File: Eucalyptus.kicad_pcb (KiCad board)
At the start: 2 copper layers, 60 x 35 mm, 59 parts, among them J1 HEADER_2, J10 ICSP, J11 HEADER_1, J12 HEADER_1, J13 HEADER_1, J14 HEADER_1, J15 HEADER_1, J16 HEADER_2, J17 HEADER_2, J2 Transmisor RF, J3 HEADER_1, J4 HEADER_1, J5 HEADER_1, J6 HEADER_1, J7 HEADER_1, J8 HEADER_1, J9 HEADER_1, Q1 2N7002, SW1 SW_PUSH, SW2 SW_PUSH, SW3 Estrategias, U1 LM1117-SOT, U2 ATMEGA328P-AU, U3 DRV8872, U4 DRV8872, Y1 Crystal

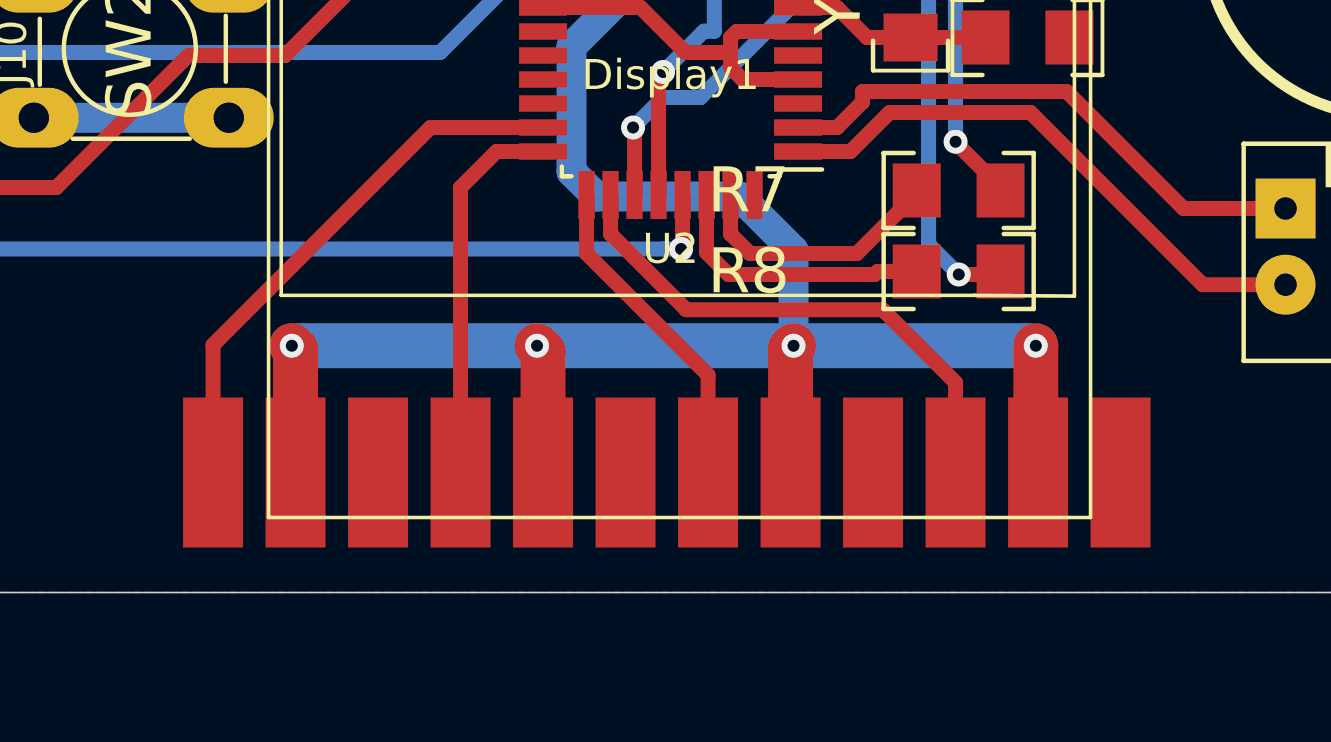
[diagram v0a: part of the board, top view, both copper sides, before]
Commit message: DualPad
Modifique y acomode los footprints de los sensores
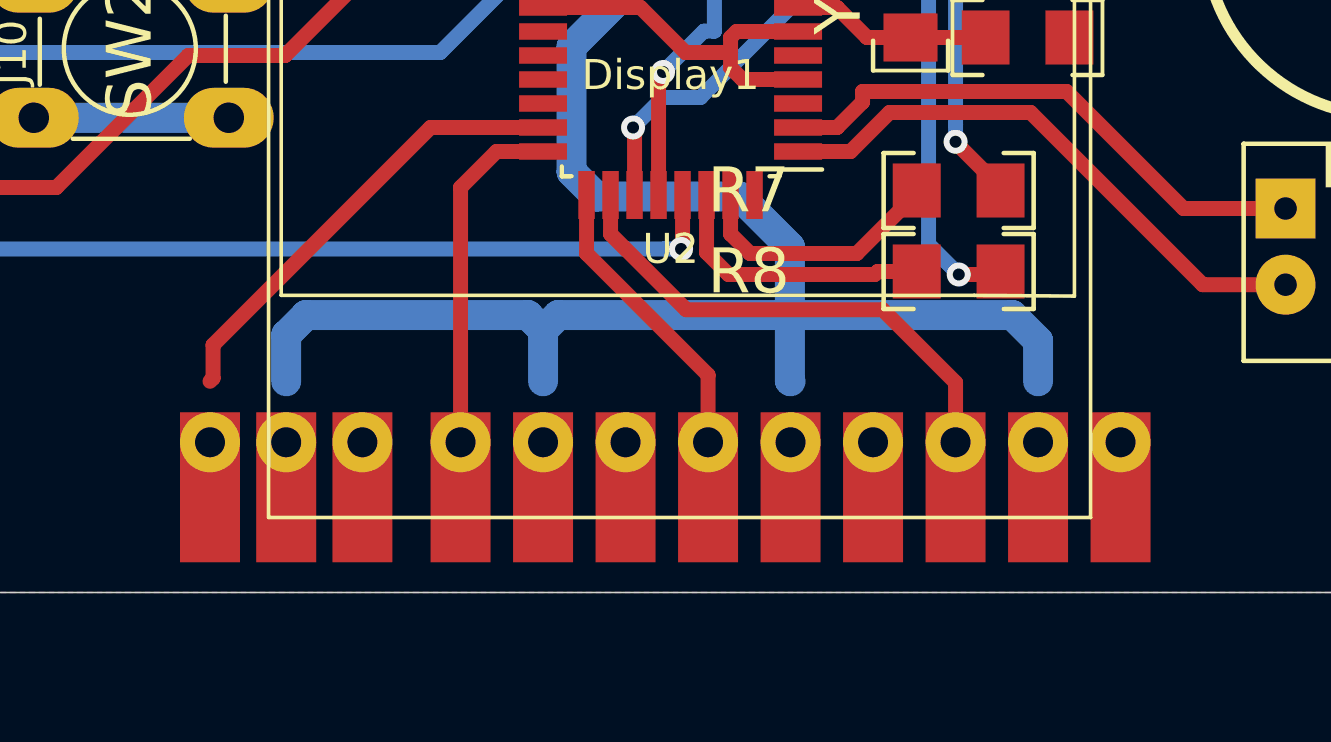
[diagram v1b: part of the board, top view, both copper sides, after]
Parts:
- J11, J12, J13, J14, J15, J3, J4, J5, J6, J7, J8, J9: footprint EESTN5:PAD_SMD_2x5mm -> EESTN5:DUAL_PAD_TH_SMD_2x5mm
- moved J9 0.72 mm to (109.7, 126.5), turned to 0 degrees
- moved J11 0.58 mm to (107.2, 126.5), turned to 0 degrees
- moved J5 0.50 mm to (104.6, 126.5)
- moved J12 0.49 mm to (121.2, 126.5)
- moved J13 0.49 mm to (118.5, 126.5), turned to 0 degrees
- moved J14 0.49 mm to (115.8, 126.5), turned to 0 degrees
- moved J15 0.49 mm to (113.0, 126.5)
- moved J3 0.49 mm to (135.0, 126.5)
- moved J4 0.49 mm to (132.2, 126.5)
- moved J6 0.49 mm to (126.8, 126.5)
- moved J7 0.49 mm to (124.0, 126.5)
- moved J8 0.49 mm to (129.5, 126.5)
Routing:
- net +5V: track 115.9 -> 106.0 mm, vias 4 -> 0
- net /DISTANCIA_I: track 19.3 -> 15.3 mm
- net /DISTANCIA_FI: track 13.7 -> 11.2 mm
- net /DISTANCIA_FD: track 11.9 -> 9.39 mm
- net /DISTANCIA_D: track 18.9 -> 16.3 mm

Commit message: MODIFICACIONES
SE MODIFICO LISTA DE MATERIALES Y EL PCB
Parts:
- C1, C11, C13, C14, C15, C3, D1, R10, R4, R5, R9, U1: moved to B.Cu
- moved C6 137.5 mm to (46.9, 99.8)
- moved R3 137.5 mm to (46.9, 103.5)
- moved SW1 113.8 mm to (166.4, 121.9), turned to 90 degrees
- moved C3 113.4 mm to (103.3, 104.1), turned to 90 degrees
- moved C11 110.5 mm to (100.5, 104.3), turned to 270 degrees
- moved C15 96.2 mm to (111.2, 101.7), turned to 90 degrees
- moved R10 94.6 mm to (121.3, 115.3), turned to 270 degrees
- moved U1 89.7 mm to (137.1, 102.8), turned to 90 degrees
- moved C14 82.0 mm to (140.8, 110.9)
- moved C13 66.6 mm to (135.4, 110.0), turned to 90 degrees
- moved C1 61.9 mm to (172.2, 100.5)
- moved R5 48.8 mm to (134.4, 119.9), turned to 270 degrees
- moved R4 46.0 mm to (136.9, 119.9), turned to 270 degrees
- moved R9 22.2 mm to (120.1, 108.2), turned to 180 degrees
- moved D1 13.7 mm to (144.0, 108.2), turned to 180 degrees
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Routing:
- net +5V: track 106.0 -> 144.2 mm
- net Net-(BZ1-Pad2): track 16.4 -> 2.98 mm
- net /AUX2: track 18.6 -> 27.0 mm
- net /Vin: track 53.7 -> 61.5 mm
- net /AUX1: track 19.2 -> 23.6 mm
- net /DISTANCIA_I: track 15.3 -> 18.8 mm
- net /BUZZER: track 1.99 -> 0.00 mm
- net /SDA: track 17.8 -> 19.2 mm

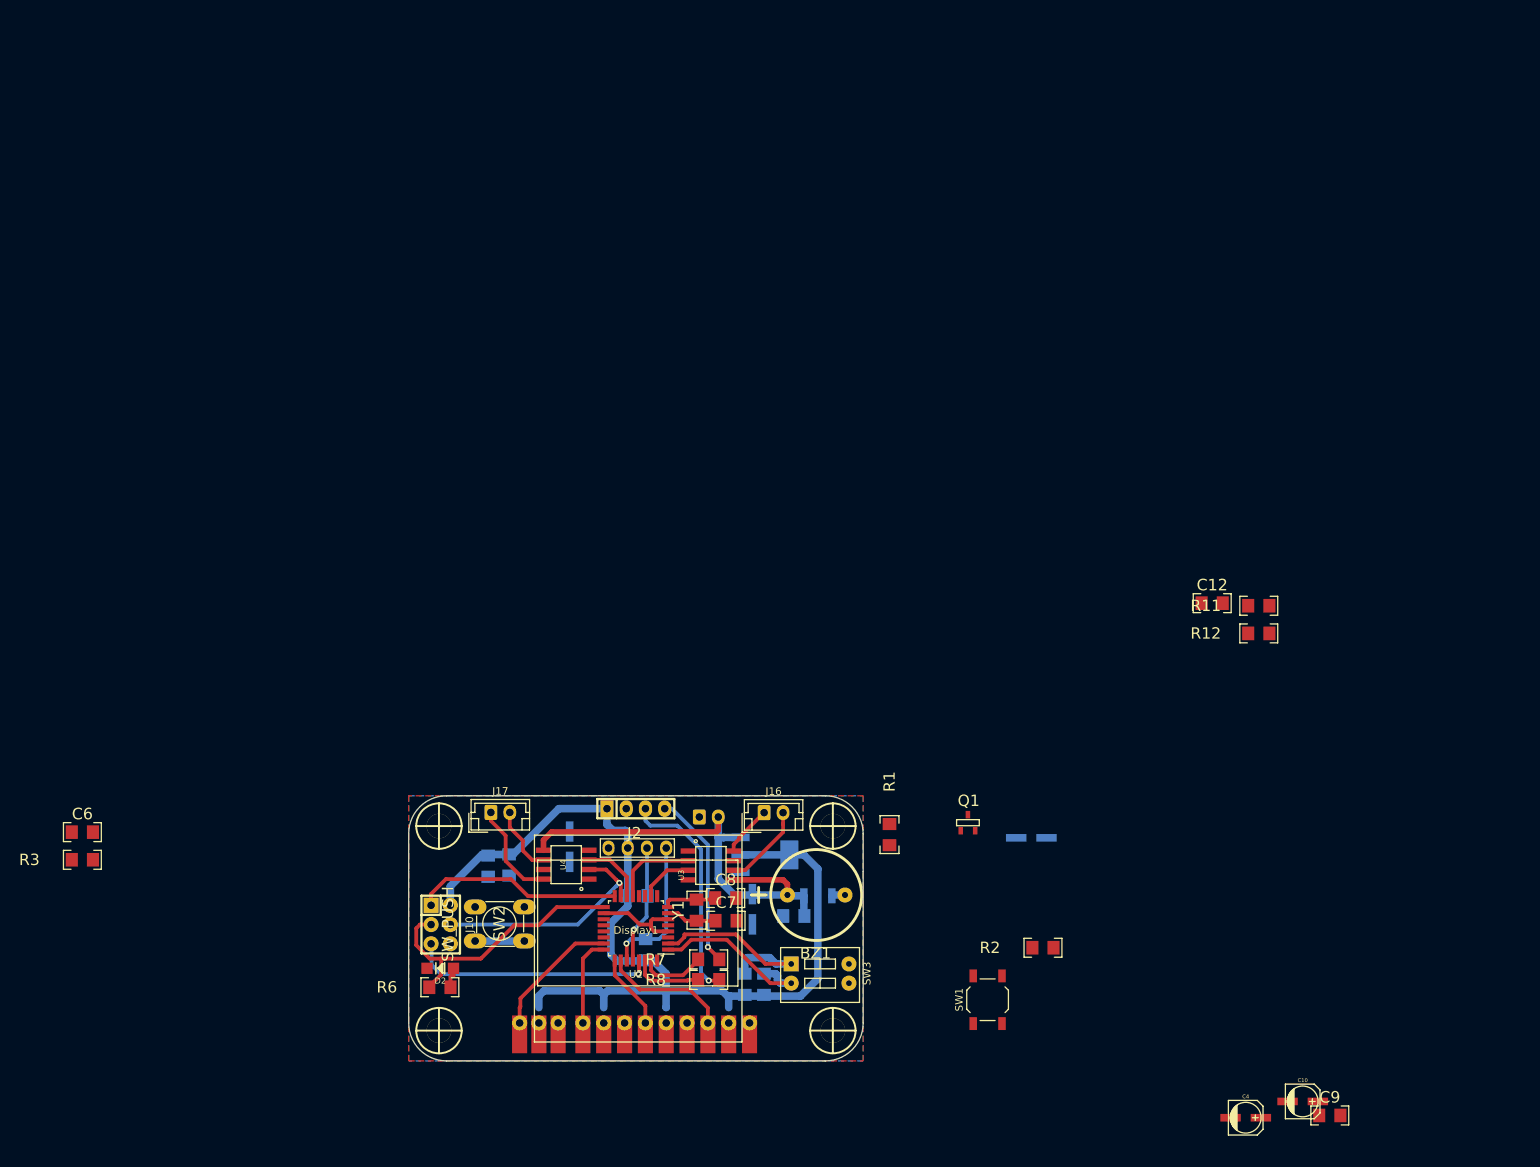
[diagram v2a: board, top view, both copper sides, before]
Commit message: modificaciones
se termino el pcb, modifique el cristal en e sch, termine lista de compnentes y genere 2 imagenes de la pcb
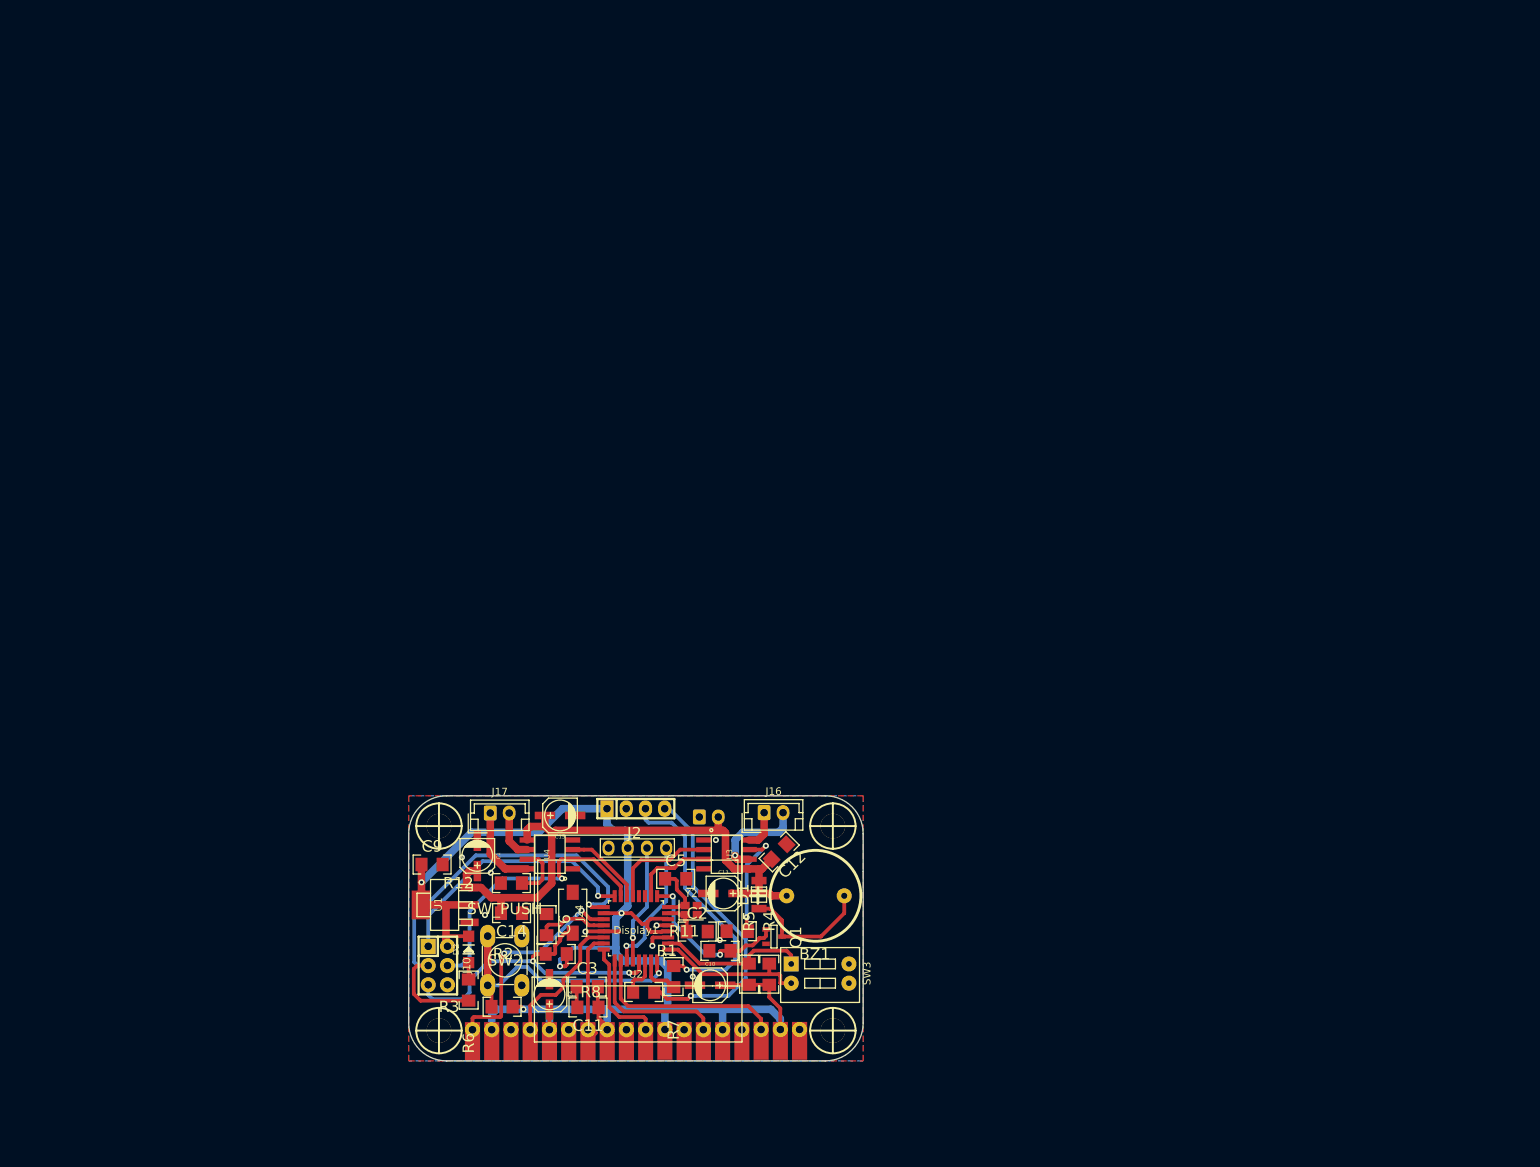
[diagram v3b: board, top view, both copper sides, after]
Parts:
- removed C7, C8: 18pF, EESTN5:C_1206
- removed R10, R9: R, EESTN5:R_1206
- removed SW1: SW_PUSH, Button_Switch_SMD:SW_SPST_TL3342
- removed Y1: Crystal, EESTN5:C_1206
- added C2: 18pF, EESTN5:C_1206, F.Cu at (128.1, 112.9)
- added C5: 18pF, EESTN5:C_1206, F.Cu at (125.2, 106.0)
- added J18: HEADER_1, EESTN5:DUAL_PAD_TH_SMD_2x5mm, F.Cu at (103.5, 127.4)
- added J19: HEADER_1, EESTN5:DUAL_PAD_TH_SMD_2x5mm, F.Cu at (101.0, 127.4)
- added J20: HEADER_1, EESTN5:DUAL_PAD_TH_SMD_2x5mm, F.Cu at (98.4, 127.4)
- added J21: HEADER_1, EESTN5:DUAL_PAD_TH_SMD_2x5mm, F.Cu at (111.1, 127.4)
- added J22: HEADER_1, EESTN5:DUAL_PAD_TH_SMD_2x5mm, F.Cu at (108.6, 127.4)
- added J23: HEADER_1, EESTN5:DUAL_PAD_TH_SMD_2x5mm, F.Cu at (106.0, 127.4)
- added J24: HEADER_2, EESTN5:SW_SPST_EVQPE1, F.Cu at (111.7, 110.4)
- added Y2: Crystal_GND23_Small, Crystal:Crystal_SMD_EuroQuartz_X22-4Pin_2.5x2.0mm, F.Cu at (127.3, 110.1)
- C1, C11, C3, D1, R4, R5, U1: moved to F.Cu
- C12: value C -> 100nf
- C13, C15: value CAPAPOL -> 100uf; moved to F.Cu
- C14: value C -> 100nf; moved to F.Cu
- J16, J17: value HEADER_2 -> motores
- R11, R12: value 0,,25 -> 0,25
- moved C9 123.1 mm to (93.1, 104.1)
- moved R12 104.0 mm to (103.6, 106.5)
- moved C4 93.3 mm to (108.6, 121.2), turned to 270 degrees
- moved R11 81.2 mm to (133.4, 112.9)
- moved C10 79.7 mm to (129.8, 120.0)
- moved C1 73.2 mm to (99.1, 102.9), turned to 270 degrees
- moved C12 65.9 mm to (138.9, 102.4), turned to 225 degrees
- moved R2 64.3 mm to (109.5, 115.9)
- moved C6 62.5 mm to (108.2, 112.0), turned to 270 degrees
- moved R3 58.7 mm to (102.3, 122.8)
- moved U1 42.9 mm to (94.7, 109.4)
- moved C14 37.3 mm to (103.6, 110.5), turned to 180 degrees
- moved Q1 29.7 mm to (138.2, 113.6), turned to 270 degrees
- moved R1 27.1 mm to (131.1, 115.5), turned to 0 degrees
- moved C11 22.8 mm to (113.7, 122.9), turned to 180 degrees
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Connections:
- J2 pad 3: /Rx -> /Tx
- J2 pad 4: /Tx -> /Rx
- U2 pad 19: (no net) -> /TATAMI_TI
- U2 pad 22: (no net) -> /TATAMI_TD
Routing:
- net +5V: track 144.2 -> 189.2 mm, vias 0 -> 4
- net /TATAMI_TI: track 0.00 -> 31.3 mm, vias 0 -> 2
- net /START: track 6.50 -> 36.1 mm, vias 0 -> 1
- net /BUZZER: track 0.00 -> 21.7 mm, vias 0 -> 2
- net /D13/SCK: track 37.2 -> 58.3 mm, vias 0 -> 1
- net /TATAMI_TD: track 0.00 -> 20.0 mm
- net /Vin: track 61.5 -> 77.2 mm
- net Net-(R11-Pad1): track 0.00 -> 14.8 mm, vias 0 -> 2
- net Net-(BZ1-Pad2): track 2.98 -> 17.6 mm
- net /Tx: track 23.4 -> 35.5 mm
- net GND: track 0.00 -> 11.9 mm, vias 0 -> 9
- net /DISTANCIA_FD: track 9.39 -> 21.1 mm
- net /Rx: track 29.7 -> 40.8 mm
- net /RESET: track 32.5 -> 42.4 mm, vias 1 -> 2
- net /DISTANCIA_D: track 16.3 -> 26.1 mm
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
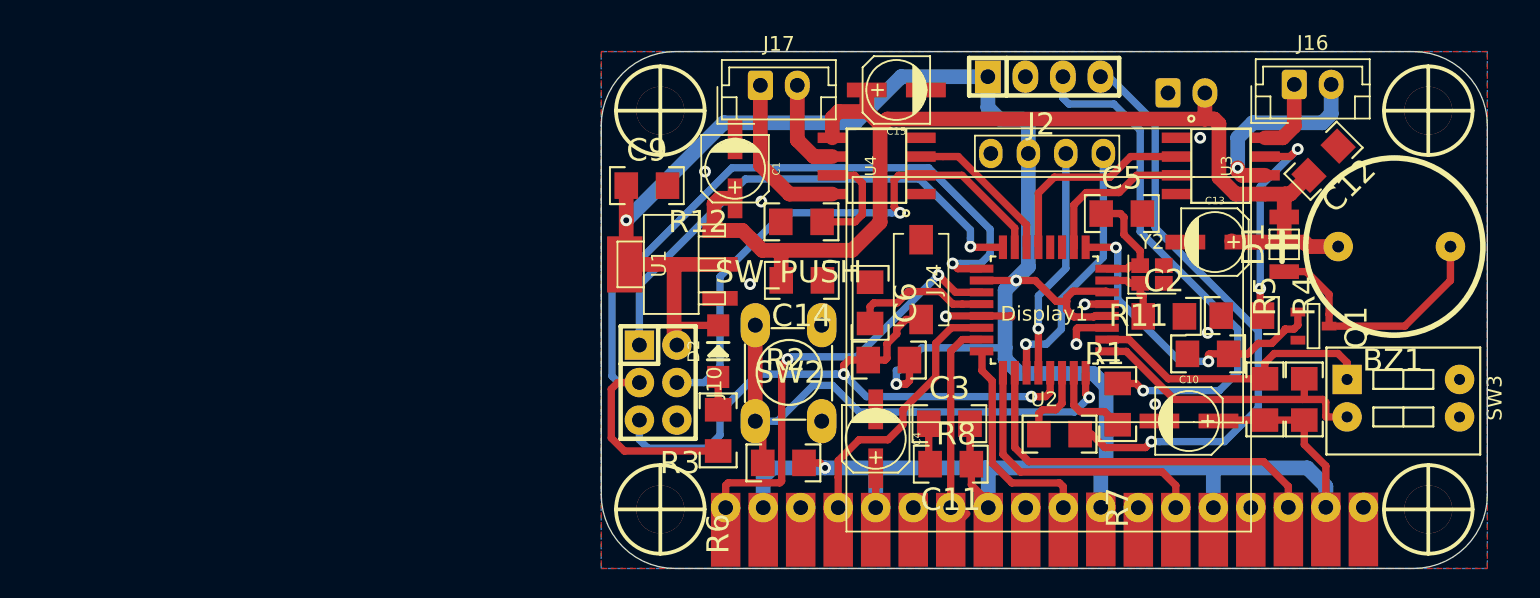
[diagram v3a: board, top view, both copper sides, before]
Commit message: modificaciones
se agrego logos,imagenes de referencias y se modifico serigrafia
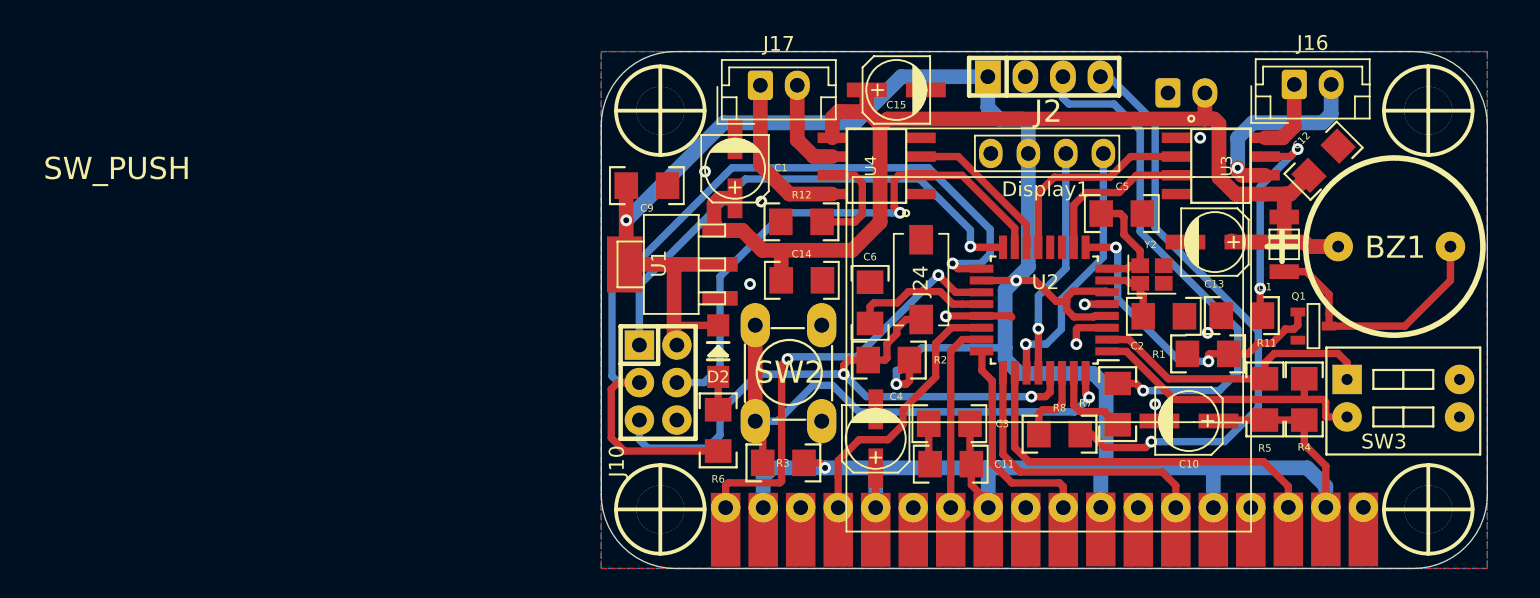
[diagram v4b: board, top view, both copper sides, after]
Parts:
- added G***: LOGO, logo:c, B.Cu at (109.3, 102.1)
- added G***: LOGO, logo:log02, B.Cu at (94.0, 107.3)
